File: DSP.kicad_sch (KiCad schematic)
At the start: 19 parts, among them J2 Conn_01x04, J4 Conn_01x04, J5 Conn_01x04, J7 Conn_01x06, U4 STM32F401RBTx, Y1 16MHz

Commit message: changed footprint of caps
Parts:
- C14, C15, C16, C17, C18, C22: value 100n -> (none); footprint Capacitor_SMD:C_0603_1608Metric_Pad1.08x0.95mm_HandSolder -> (none)
- C19, C36: value 10u -> (none); footprint Capacitor_SMD:C_0603_1608Metric_Pad1.08x0.95mm_HandSolder -> (none)
- C20, C21: value 10p -> (none); footprint Capacitor_SMD:C_0603_1608Metric_Pad1.08x0.95mm_HandSolder -> (none)
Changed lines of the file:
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@@
       (effects (font (size 1.27 1.27)) (justify left))
     )
-    (property "Value" "10p" (id 1) (at 81.28 96.52 90)
-      (effects (font (size 1.27 1.27)) (justify left))
-    )
-    (property "Footprint" "Capacitor_SMD:C_0603_1608Metric_Pad1.08x0.95mm_HandSolder" (id 2) (at 83.82 91.44 0)
+    (property "Value" "" (id 1) (at 81.28 96.52 90)
+      (effects (font (size 1.27 1.27)) (justify left))
+    )
+    (property "Footprint" "" (id 2) (at 83.82 91.44 0)
       (effects (font (size 1.27 1.27)) hide)
     )
@@
       (effects (font (size 1.27 1.27)) (justify left))
     )
-    (property "Value" "10p" (id 1) (at 62.23 96.52 90)
-      (effects (font (size 1.27 1.27)) (justify left))
-    )
-    (property "Footprint" "Capacitor_SMD:C_0603_1608Metric_Pad1.08x0.95mm_HandSolder" (id 2) (at 64.77 91.44 0)
+    (property "Value" "" (id 1) (at 62.23 96.52 90)
+      (effects (font (size 1.27 1.27)) (justify left))
+    )
+    (property "Footprint" "" (id 2) (at 64.77 91.44 0)
       (effects (font (size 1.27 1.27)) hide)
     )
@@
       (effects (font (size 1.27 1.27)) (justify left))
     )
-    (property "Value" "100n" (id 1) (at 78.74 33.02 0)
-      (effects (font (size 1.27 1.27)) (justify left))
-    )
-    (property "Footprint" "Capacitor_SMD:C_0603_1608Metric_Pad1.08x0.95mm_HandSolder" (id 2) (at 85.09 31.75 0)
+    (property "Value" "" (id 1) (at 78.74 33.02 0)
+      (effects (font (size 1.27 1.27)) (justify left))
+    )
+    (property "Footprint" "" (id 2) (at 85.09 31.75 0)
       (effects (font (size 1.27 1.27)) hide)
     )
@@
       (effects (font (size 1.27 1.27)) (justify left))
     )
-    (property "Value" "100n" (id 1) (at 175.26 45.72 90)
-      (effects (font (size 1.27 1.27)) (justify left))
-    )
-    (property "Footprint" "Capacitor_SMD:C_0603_1608Metric_Pad1.08x0.95mm_HandSolder" (id 2) (at 177.8 40.64 0)
+    (property "Value" "" (id 1) (at 175.26 45.72 90)
+      (effects (font (size 1.27 1.27)) (justify left))
+    )
+    (property "Footprint" "" (id 2) (at 177.8 40.64 0)
       (effects (font (size 1.27 1.27)) hide)
     )
@@
       (effects (font (size 1.27 1.27)) (justify left))
     )
-    (property "Value" "100n" (id 1) (at 165.1 45.72 90)
-      (effects (font (size 1.27 1.27)) (justify left))
-    )
-    (property "Footprint" "Capacitor_SMD:C_0603_1608Metric_Pad1.08x0.95mm_HandSolder" (id 2) (at 167.64 40.64 0)
+    (property "Value" "" (id 1) (at 165.1 45.72 90)
+      (effects (font (size 1.27 1.27)) (justify left))
+    )
+    (property "Footprint" "" (id 2) (at 167.64 40.64 0)
       (effects (font (size 1.27 1.27)) hide)
     )
@@
       (effects (font (size 1.27 1.27)) (justify left))
     )
-    (property "Value" "100n" (id 1) (at 154.94 45.72 90)
-      (effects (font (size 1.27 1.27)) (justify left))
-    )
-    (property "Footprint" "Capacitor_SMD:C_0603_1608Metric_Pad1.08x0.95mm_HandSolder" (id 2) (at 157.48 40.64 0)
+    (property "Value" "" (id 1) (at 154.94 45.72 90)
+      (effects (font (size 1.27 1.27)) (justify left))
+    )
+    (property "Footprint" "" (id 2) (at 157.48 40.64 0)
       (effects (font (size 1.27 1.27)) hide)
     )
@@
       (effects (font (size 1.27 1.27)) (justify left))
     )
-    (property "Value" "100n" (id 1) (at 170.18 45.72 90)
-      (effects (font (size 1.27 1.27)) (justify left))
-    )
-    (property "Footprint" "Capacitor_SMD:C_0603_1608Metric_Pad1.08x0.95mm_HandSolder" (id 2) (at 172.72 40.64 0)
+    (property "Value" "" (id 1) (at 170.18 45.72 90)
+      (effects (font (size 1.27 1.27)) (justify left))
+    )
+    (property "Footprint" "" (id 2) (at 172.72 40.64 0)
       (effects (font (size 1.27 1.27)) hide)
     )
@@
       (effects (font (size 1.27 1.27)) (justify left))
     )
-    (property "Value" "10u" (id 1) (at 78.74 57.15 0)
-      (effects (font (size 1.27 1.27)) (justify left))
-    )
-    (property "Footprint" "Capacitor_SMD:C_0603_1608Metric_Pad1.08x0.95mm_HandSolder" (id 2) (at 83.82 55.88 0)
+    (property "Value" "" (id 1) (at 78.74 57.15 0)
+      (effects (font (size 1.27 1.27)) (justify left))
+    )
+    (property "Footprint" "" (id 2) (at 83.82 55.88 0)
       (effects (font (size 1.27 1.27)) hide)
     )
@@
       (effects (font (size 1.27 1.27)) (justify left))
     )
-    (property "Value" "100n" (id 1) (at 160.02 45.72 90)
-      (effects (font (size 1.27 1.27)) (justify left))
-    )
-    (property "Footprint" "Capacitor_SMD:C_0603_1608Metric_Pad1.08x0.95mm_HandSolder" (id 2) (at 162.56 40.64 0)
+    (property "Value" "" (id 1) (at 160.02 45.72 90)
+      (effects (font (size 1.27 1.27)) (justify left))
+    )
+    (property "Footprint" "" (id 2) (at 162.56 40.64 0)
       (effects (font (size 1.27 1.27)) hide)
     )
@@
       (effects (font (size 1.27 1.27)) (justify left))
     )
-    (property "Value" "10u" (id 1) (at 180.34 45.72 90)
-      (effects (font (size 1.27 1.27)) (justify left))
-    )
-    (property "Footprint" "Capacitor_SMD:C_0603_1608Metric_Pad1.08x0.95mm_HandSolder" (id 2) (at 182.88 40.64 0)
-      (effects (font (size 1.27 1.27)) hide)
-    )
+    (property "Value" "" (id 1) (at 180.34 45.72 90)
+      (effects (font (size 1.27 1.27)) (justify left))
+    )
+    (property "Footprint" "" (id 2) (at 182.88 40.64 0)
+      (effects (font (size 1.27 1.27)) hide)
+    )

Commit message: grounded mounting holes gnd top layer polygon and cool looking gnd strips on analog side
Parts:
- C14, C15, C16, C17, C18, C22: value (none) -> 100n; footprint (none) -> Capacitor_SMD:C_0603_1608Metric_Pad1.08x0.95mm_HandSolder
- C19, C36: value (none) -> 10u; footprint (none) -> Capacitor_SMD:C_0603_1608Metric_Pad1.08x0.95mm_HandSolder
- C20, C21: value (none) -> 10p; footprint (none) -> Capacitor_SMD:C_0603_1608Metric_Pad1.08x0.95mm_HandSolder
- D2: value R -> Green
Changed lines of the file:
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@@
       (effects (font (size 1.27 1.27)) (justify left))
     )
-    (property "Value" "" (id 1) (at 81.28 96.52 90)
-      (effects (font (size 1.27 1.27)) (justify left))
-    )
-    (property "Footprint" "" (id 2) (at 83.82 91.44 0)
+    (property "Value" "10p" (id 1) (at 81.28 96.52 90)
+      (effects (font (size 1.27 1.27)) (justify left))
+    )
+    (property "Footprint" "Capacitor_SMD:C_0603_1608Metric_Pad1.08x0.95mm_HandSolder" (id 2) (at 83.82 91.44 0)
       (effects (font (size 1.27 1.27)) hide)
     )
@@
       (effects (font (size 1.27 1.27)) (justify left))
     )
-    (property "Value" "" (id 1) (at 62.23 96.52 90)
-      (effects (font (size 1.27 1.27)) (justify left))
-    )
-    (property "Footprint" "" (id 2) (at 64.77 91.44 0)
+    (property "Value" "10p" (id 1) (at 62.23 96.52 90)
+      (effects (font (size 1.27 1.27)) (justify left))
+    )
+    (property "Footprint" "Capacitor_SMD:C_0603_1608Metric_Pad1.08x0.95mm_HandSolder" (id 2) (at 64.77 91.44 0)
       (effects (font (size 1.27 1.27)) hide)
     )
@@
       (effects (font (size 1.27 1.27)) (justify left))
     )
-    (property "Value" "" (id 1) (at 78.74 33.02 0)
-      (effects (font (size 1.27 1.27)) (justify left))
-    )
-    (property "Footprint" "" (id 2) (at 85.09 31.75 0)
+    (property "Value" "100n" (id 1) (at 78.74 33.02 0)
+      (effects (font (size 1.27 1.27)) (justify left))
+    )
+    (property "Footprint" "Capacitor_SMD:C_0603_1608Metric_Pad1.08x0.95mm_HandSolder" (id 2) (at 85.09 31.75 0)
       (effects (font (size 1.27 1.27)) hide)
     )
@@
       (effects (font (size 1.27 1.27)) (justify right))
     )
-    (property "Value" "R" (id 1) (at 91.44 129.4764 90)
+    (property "Value" "Green" (id 1) (at 91.44 129.4764 90)
       (effects (font (size 1.27 1.27)) (justify right))
     )
@@
       (effects (font (size 1.27 1.27)) (justify left))
     )
-    (property "Value" "" (id 1) (at 175.26 45.72 90)
-      (effects (font (size 1.27 1.27)) (justify left))
-    )
-    (property "Footprint" "" (id 2) (at 177.8 40.64 0)
+    (property "Value" "100n" (id 1) (at 175.26 45.72 90)
+      (effects (font (size 1.27 1.27)) (justify left))
+    )
+    (property "Footprint" "Capacitor_SMD:C_0603_1608Metric_Pad1.08x0.95mm_HandSolder" (id 2) (at 177.8 40.64 0)
       (effects (font (size 1.27 1.27)) hide)
     )
@@
       (effects (font (size 1.27 1.27)) (justify left))
     )
-    (property "Value" "" (id 1) (at 165.1 45.72 90)
-      (effects (font (size 1.27 1.27)) (justify left))
-    )
-    (property "Footprint" "" (id 2) (at 167.64 40.64 0)
+    (property "Value" "100n" (id 1) (at 165.1 45.72 90)
+      (effects (font (size 1.27 1.27)) (justify left))
+    )
+    (property "Footprint" "Capacitor_SMD:C_0603_1608Metric_Pad1.08x0.95mm_HandSolder" (id 2) (at 167.64 40.64 0)
       (effects (font (size 1.27 1.27)) hide)
     )
@@
       (effects (font (size 1.27 1.27)) (justify left))
     )
-    (property "Value" "" (id 1) (at 154.94 45.72 90)
-      (effects (font (size 1.27 1.27)) (justify left))
-    )
-    (property "Footprint" "" (id 2) (at 157.48 40.64 0)
+    (property "Value" "100n" (id 1) (at 154.94 45.72 90)
+      (effects (font (size 1.27 1.27)) (justify left))
+    )
+    (property "Footprint" "Capacitor_SMD:C_0603_1608Metric_Pad1.08x0.95mm_HandSolder" (id 2) (at 157.48 40.64 0)
       (effects (font (size 1.27 1.27)) hide)
     )
@@
       (effects (font (size 1.27 1.27)) (justify left))
     )
-    (property "Value" "" (id 1) (at 170.18 45.72 90)
-      (effects (font (size 1.27 1.27)) (justify left))
-    )
-    (property "Footprint" "" (id 2) (at 172.72 40.64 0)
+    (property "Value" "100n" (id 1) (at 170.18 45.72 90)
+      (effects (font (size 1.27 1.27)) (justify left))
+    )
+    (property "Footprint" "Capacitor_SMD:C_0603_1608Metric_Pad1.08x0.95mm_HandSolder" (id 2) (at 172.72 40.64 0)
       (effects (font (size 1.27 1.27)) hide)
     )
@@
       (effects (font (size 1.27 1.27)) (justify left))
     )
-    (property "Value" "" (id 1) (at 78.74 57.15 0)
-      (effects (font (size 1.27 1.27)) (justify left))
-    )
-    (property "Footprint" "" (id 2) (at 83.82 55.88 0)
+    (property "Value" "10u" (id 1) (at 78.74 57.15 0)
+      (effects (font (size 1.27 1.27)) (justify left))
+    )
+    (property "Footprint" "Capacitor_SMD:C_0603_1608Metric_Pad1.08x0.95mm_HandSolder" (id 2) (at 83.82 55.88 0)
       (effects (font (size 1.27 1.27)) hide)
     )
@@
       (effects (font (size 1.27 1.27)) (justify left))
     )
-    (property "Value" "" (id 1) (at 160.02 45.72 90)
-      (effects (font (size 1.27 1.27)) (justify left))
-    )
-    (property "Footprint" "" (id 2) (at 162.56 40.64 0)
+    (property "Value" "100n" (id 1) (at 160.02 45.72 90)
+      (effects (font (size 1.27 1.27)) (justify left))
+    )
+    (property "Footprint" "Capacitor_SMD:C_0603_1608Metric_Pad1.08x0.95mm_HandSolder" (id 2) (at 162.56 40.64 0)
       (effects (font (size 1.27 1.27)) hide)
     )
@@
       (effects (font (size 1.27 1.27)) (justify left))
     )
-    (property "Value" "" (id 1) (at 180.34 45.72 90)
-      (effects (font (size 1.27 1.27)) (justify left))
-    )
-    (property "Footprint" "" (id 2) (at 182.88 40.64 0)
-      (effects (font (size 1.27 1.27)) hide)
-    )
+    (property "Value" "10u" (id 1) (at 180.34 45.72 90)
+      (effects (font (size 1.27 1.27)) (justify left))
+    )
+    (property "Footprint" "Capacitor_SMD:C_0603_1608Metric_Pad1.08x0.95mm_HandSolder" (id 2) (at 182.88 40.64 0)
+      (effects (font (size 1.27 1.27)) hide)
+    )

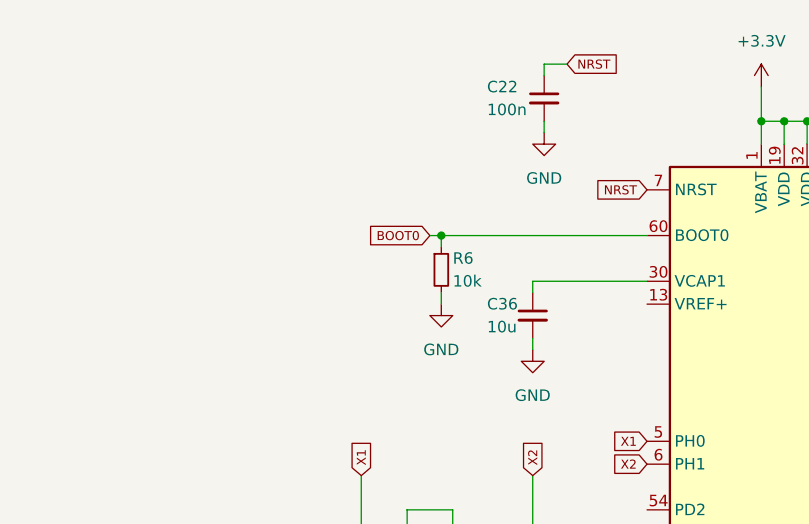
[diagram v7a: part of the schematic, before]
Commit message: added boot and reset button
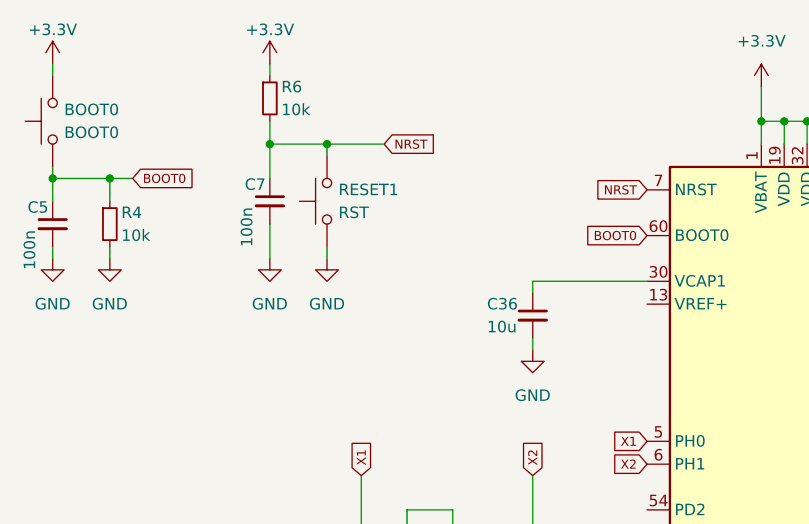
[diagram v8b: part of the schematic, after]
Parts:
- removed C22: 100n, Capacitor_SMD:C_0603_1608Metric_Pad1.08x0.95mm_HandSolder, symbol Device:C_Small
- added BOOT0: BOOT0, Button_Switch_SMD:SW_SPST_TL3342, symbol Switch:SW_Push
- added C5, C7: 100n, Capacitor_SMD:C_0603_1608Metric_Pad1.08x0.95mm_HandSolder, symbol Device:C_Small
- added R4: 10k, Resistor_SMD:R_0603_1608Metric_Pad0.98x0.95mm_HandSolder, symbol Device:R_Small
- added RESET1: RST, Button_Switch_SMD:SW_SPST_TL3342, symbol Switch:SW_Push
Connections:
- net +3V3: now also R6.1, BOOT0.2
- net BOOT0: now also BOOT0.1, C5.1, R4.1; no longer R6.1
- net GND: now also C5.2, C7.2, R4.2, RESET1.1; no longer R6.2
- net NRST: now also R6.2, C7.1, RESET1.2
